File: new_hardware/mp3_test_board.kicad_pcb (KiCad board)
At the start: 4 copper layers, 100 x 56 mm, 219 parts, among them J1 TF01-A, J2 PJ-322, P1 WF24LTYAJDNN0#, P2 USB-TYPE-C-018, Q1 2N7002K, SW1 K2-1156SP-F5SW-05, SW2 K2-1156SP-F5SW-05, SW3 K2-1156SP-F5SW-05, SW4 K2-1156SP-F5SW-05, SW5 K2-1156SP-F5SW-05, SW6 GT-TC054A-H035-L1, SW7 GT-TC054A-H035-L1, SW8 GT-TC054A-H035-L1, U1 F133, U10 SGM6603-ADJYN6G, U11 SGM3204, U2 USBLC6-2SC6, U3 MX25L25645GM2I-08G, U4 PCM1795, U5 LM4562, U6 LM4562, U7 OPA1656, U8 OPA1656, U9 AXP2101, Y1 12.88727

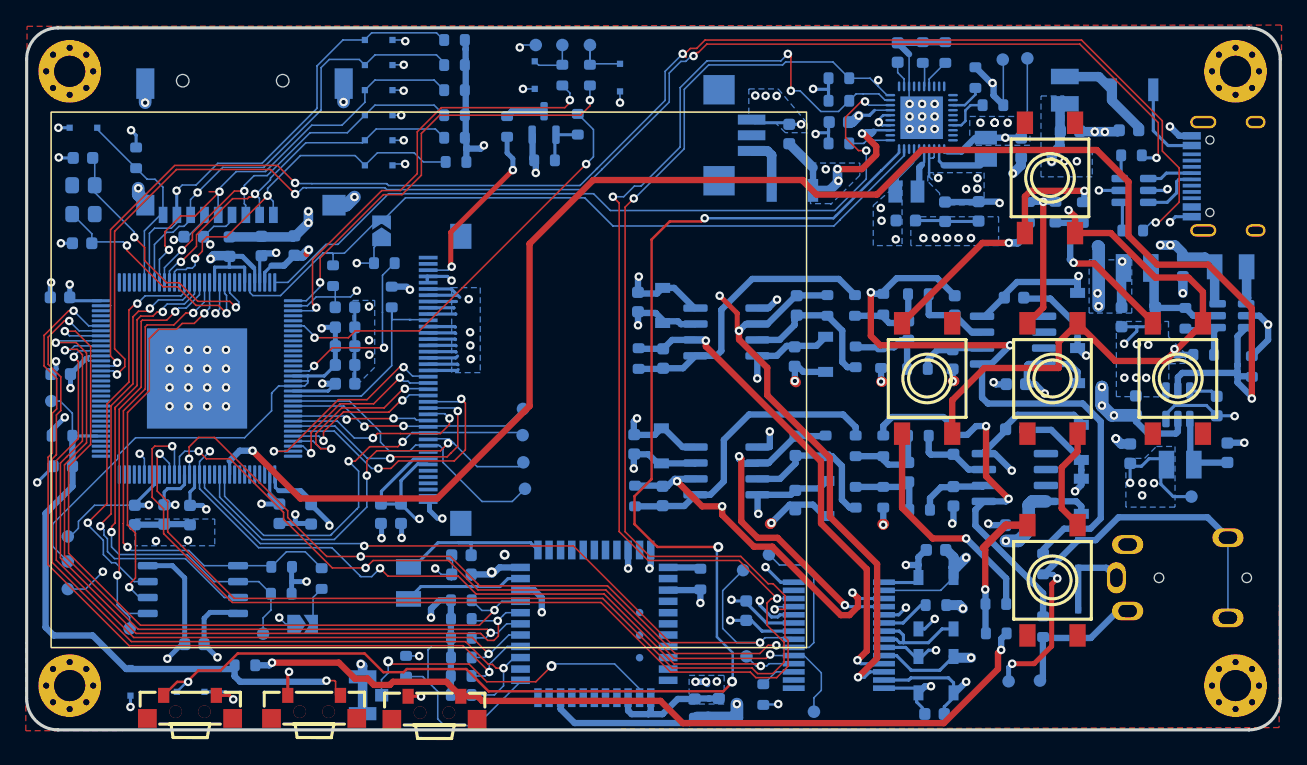
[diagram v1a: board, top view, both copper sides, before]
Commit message: wi-fi module is moved to closer board outline,unused files are removed
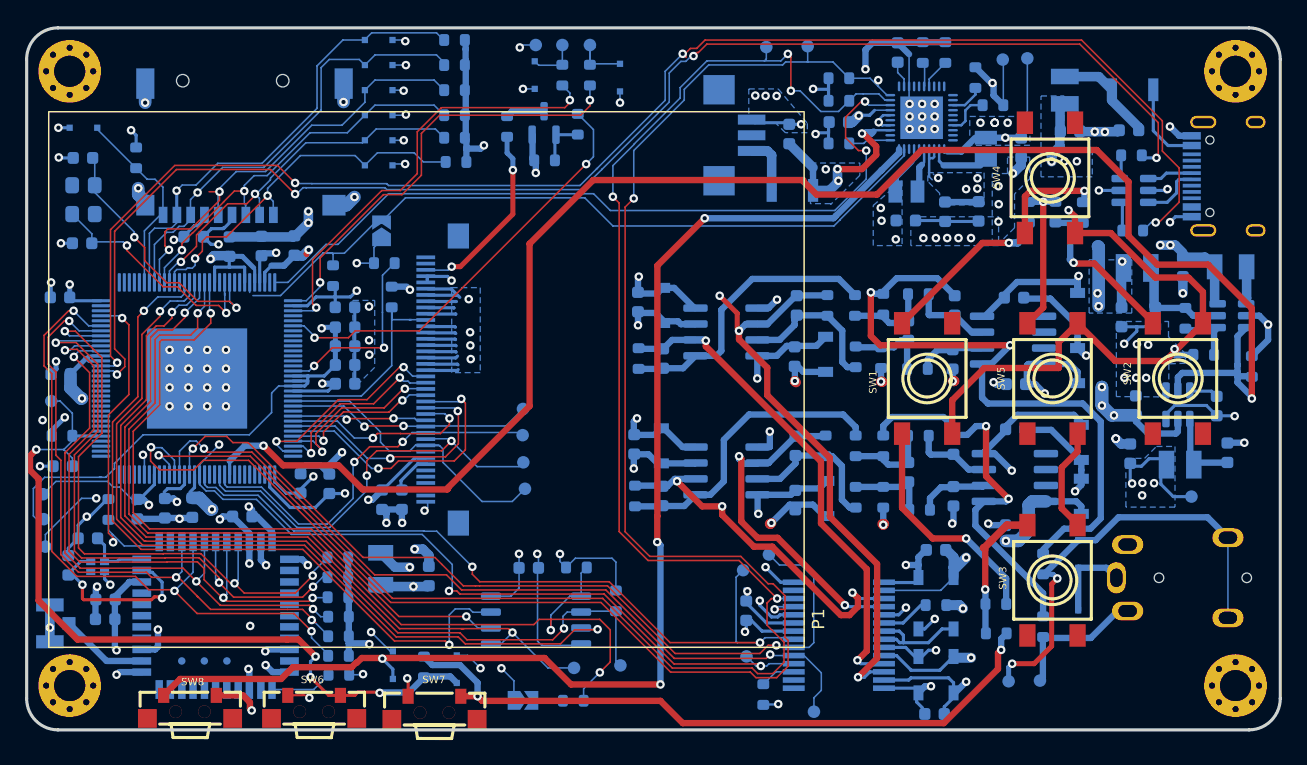
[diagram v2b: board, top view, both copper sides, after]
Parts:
- added C76: 18p, rlib_passive:C_0603_1608Metric, B.Cu at (79.8, 86.1)
- added C77: 18p, rlib_passive:C_0603_1608Metric, B.Cu at (81.4, 84.0)
- added TP24: TestPoint, TestPoint:TestPoint_Pad_D1.0mm, B.Cu at (135.5, 44.8)
- added TP25: TestPoint, TestPoint:TestPoint_Pad_D1.0mm, B.Cu at (138.8, 44.7)
- added Y2: 26МHz, rlib_passive:CRYSTAL-SMD_4P-L1.6-W1.2-BL, B.Cu at (82.1, 86.2)
- moved C56 49.7 mm to (82.8, 88.8), turned to 180 degrees
- moved C59 47.6 mm to (82.7, 90.4), turned to 180 degrees
- moved TP12 35.6 mm to (120.1, 94.3)
- moved U 30.2 mm to (91.5, 90.1), turned to 0 degrees
- moved R63 29.8 mm to (101.4, 94.8), turned to 0 degrees
- moved TP11 28.6 mm to (123.8, 94.1)
- moved U3 27.5 mm to (117.1, 90.5)
- moved C26 27.4 mm to (116.5, 86.3)
- moved R64 26.8 mm to (83.0, 81.7)
- moved R21 26.7 mm to (123.5, 88.9), turned to 90 degrees
- moved D1 26.0 mm to (110.8, 94.4), turned to -90 degrees
- moved RF1 25.6 mm to (79.1, 90.7)
- moved R17 23.5 mm to (120.3, 86.3), turned to 180 degrees
- moved R6 22.3 mm to (120.1, 96.9), turned to 0 degrees
- moved JP1 18.6 mm to (116.1, 96.9)
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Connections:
- R64 pad 1: /WI-FI/WIFI_REG_ON -> /SOC/WIFI_REG_ON
- R7 pad 1: /SOC/KEYS -> Net-(R7-Pad1)
- R7 pad 2: Net-(R7-Pad2) -> /SOC/KEYS
- R9 pad 1: Net-(R7-Pad2) -> Net-(R7-Pad1)
- SW7 pad 1: Net-(R7-Pad2) -> Net-(R7-Pad1)
- U pad 10: unconnected-(U12-Pad10) -> Net-(C76-Pad2)
- U pad 11: unconnected-(U12-Pad11) -> Net-(C77-Pad2)
- U pad 12: /WI-FI/WIFI_REG_ON -> /SOC/WIFI_REG_ON
- U1 pad 125: unconnected-(U1-Pad125) -> /SOC/WIFI_REG_ON
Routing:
- net Net-(R7-Pad2): track 66.8 -> 0.00 mm, vias 2 -> 0
- net Net-(R7-Pad1): track 0.00 -> 55.2 mm, vias 0 -> 2
- net /SOC/FLASH_SPI_CS: track 42.7 -> 79.1 mm, vias 2 -> 3
- net /SOC/FLASH_SPI_MOSI: track 34.9 -> 64.9 mm
- net /SOC/FLASH_SPI_MISO: track 43.3 -> 71.5 mm
- net /SOC/FLASH_SPI_WP: track 38.1 -> 66.3 mm
- net /SOC/FLASH_SPI_HOLD: track 31.6 -> 59.5 mm
- net /SOC/WIFI_REG_ON: track 0.00 -> 27.0 mm, vias 0 -> 2
- net /SOC/FLASH_SPI_CLK: track 30.7 -> 54.8 mm
- net /SOC/WIFI_SDIO_D2: track 69.2 -> 50.3 mm, vias 2 -> 3
- net Net-(RF1-Pad1): track 26.1 -> 7.97 mm, vias 2 -> 0
- net /WI-FI/WIFI_REG_ON: track 16.5 -> 0.00 mm
- net /SOC/WIFI_SDIO_D0: track 64.9 -> 49.1 mm, vias 2 -> 3
- net /SOC/WIFI_SDIO_CMD: track 61.7 -> 45.9 mm, vias 2 -> 3
- net /SOC/WIFI_SDIO_D1: track 64.3 -> 49.0 mm, vias 2 -> 3
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- removed copper zone on F.Cu, net GND
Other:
- board text added: "0,0889 мм / 0,0000 мм"
- board text added: "0,2000 мм"
- board text added: "1,6700 мм"
- board text added: "100,0000 мм x 56,0000 мм"
- board text added: "4"
- board text added: "None"
- board text added: "Габариты платы:"
- board text added: "Количество слоёв меди:"
- board text added: "Контроль импеданса:"
- board text added: "Краевой соединитель:"
- board text added: "Метал. торцы:"
- board text added: "Мин. дорожка/зазор:"
- board text added: "Мин. сверло:"
- board text added: "Нет"
- board text added: "Периферийные полу-отверстия:"
- board text added: "Покрытие меди:"
- board text added: "Толщина платы:"
- board text added: "ХАРАКТЕРИСТИКИ ПЛАТЫ"

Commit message: x
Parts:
- moved TP21 0.51 mm to (138.8, 98.0)
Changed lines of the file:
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@@
     (property "exclude_from_bom" "")
     (attr exclude_from_pos_files exclude_from_bom)
-    (fp_text reference "TP13" (at 0 1.448) (layer "B.SilkS")
+    (fp_text reference "TP13" (at 0.25 -1.736062) (layer "B.SilkS")
       (effects (font (size 0.6 0.6) (thickness 0.15)) (justify mirror))
     )
@@
     (property "exclude_from_bom" "")
     (attr exclude_from_pos_files exclude_from_bom)
-    (fp_text reference "TP23" (at 2.6 -0.2) (layer "B.SilkS")
+    (fp_text reference "TP23" (at 0.5304 1.612876) (layer "B.SilkS")
       (effects (font (size 0.6 0.6) (thickness 0.15)) (justify mirror))
     )
@@
     (property "exclude_from_bom" "")
     (attr exclude_from_pos_files exclude_from_bom)
-    (fp_text reference "TP22" (at 2.8 -0.4) (layer "B.SilkS")
+    (fp_text reference "TP22" (at 0.1004 1.552876) (layer "B.SilkS")
       (effects (font (size 0.6 0.6) (thickness 0.15)) (justify mirror))
     )
@@
     (property "Tolerance" "1%")
     (attr smd)
-    (fp_text reference "R23" (at 0 1.43 90) (layer "B.SilkS")
+    (fp_text reference "R23" (at 0.032876 -1.7404 90) (layer "B.SilkS")
       (effects (font (size 0.6 0.6) (thickness 0.15)) (justify mirror))
     )
@@
     (property "Voltage" "")
     (attr smd)
-    (fp_text reference "C4" (at -0.81 -4.39 90) (layer "B.SilkS")
+    (fp_text reference "C4" (at -0.006062 1.3573 90) (layer "B.SilkS")
       (effects (font (size 0.6 0.6) (thickness 0.15)) (justify mirror))
     )
@@
     (property "exclude_from_bom" "")
     (attr exclude_from_pos_files exclude_from_bom)
-    (fp_text reference "TP14" (at 0 1.448 90) (layer "B.SilkS")
+    (fp_text reference "TP14" (at 1.97 0.01) (layer "B.SilkS")
       (effects (font (size 0.6 0.6) (thickness 0.15)) (justify mirror))
     )
@@
     (property "Tolerance" "1%")
     (attr smd)
-    (fp_text reference "R9" (at 0 1.43) (layer "B.SilkS")
+    (fp_text reference "R9" (at 0.0627 1.163938) (layer "B.SilkS")
       (effects (font (size 0.6 0.6) (thickness 0.15)) (justify mirror))
     )
@@
     (property "Voltage" "")
     (attr smd)
-    (fp_text reference "C8" (at -0.82 -5.61 90) (layer "B.SilkS")
+    (fp_text reference "C8" (at 0.203938 1.3373 90) (layer "B.SilkS")
       (effects (font (size 0.6 0.6) (thickness 0.15)) (justify mirror))
     )
@@
     (property "Tolerance" "1%")
     (attr smd)
-    (fp_text reference "R53" (at 2.8 1.2) (layer "B.SilkS")
+    (fp_text reference "R53" (at 2.48 1) (layer "B.SilkS")
       (effects (font (size 0.6 0.6) (thickness 0.15)) (justify mirror))
     )
@@
     (property "Voltage" "")
     (attr smd)
-    (fp_text reference "C27" (at 2.8 0) (layer "B.SilkS")
+    (fp_text reference "C27" (at 2.8927 -0.026062) (layer "B.SilkS")
       (effects (font (size 0.6 0.6) (thickness 0.15)) (justify mirror))
     )
@@
     (property "Voltage" "")
     (attr smd)
-    (fp_text reference "C9" (at -0.82 -6.83 90) (layer "B.SilkS")
+    (fp_text reference "C9" (at 0.193938 1.4573 90) (layer "B.SilkS")
       (effects (font (size 0.6 0.6) (thickness 0.15)) (justify mirror))
     )
@@
   )
   (footprint "TestPoint:TestPoint_Pad_D1.0mm" (layer "B.Cu")
-    (at 139.2704 97.782876 180)
+    (at 138.8 97.99 180)
     (descr "SMD pad as test Point, diameter 1.0mm")
     (tags "test point SMD pad")
@@
     (property "exclude_from_bom" "")
     (attr exclude_from_pos_files exclude_from_bom)
-    (fp_text reference "TP21" (at 2.8 -0.2) (layer "B.SilkS")
+    (fp_text reference "TP21" (at 2.3204 -0.387124) (layer "B.SilkS")
       (effects (font (size 0.6 0.6) (thickness 0.15)) (justify mirror))
     )
@@
   (via (at 90.611862 76.798038) (size 0.6858) (drill 0.3302) (layers "F.Cu" "B.Cu") (net 168))
   (segment (start 88.66 78.8625) (end 88.66 77.006647) (width 0.127) (layer "B.Cu") (net 168))
-  (segment (start 139.8577 96.078938) (end 139.8577 94.678938) (width 0.127) (layer "B.Cu") (net 168))
+  (segment (start 138.8 97.136638) (end 139.8577 96.078938) (width 0.127) (layer "B.Cu") (net 168))
   (segment (start 88.66 77.006647) (end 89.474509 76.192138) (width 0.127) (layer "B.Cu") (net 168))
+  (segment (start 138.8 97.99) (end 138.8 97.136638) (width 0.127) (layer "B.Cu") (net 168))
+  (segment (start 139.8577 96.078938) (end 139.8577 94.678938) (width 0.127) (layer "B.Cu") (net 168))
   (segment (start 135.78 93.22) (end 135.863938 93.303938) (width 0.127) (layer "B.Cu") (net 168))
-  (segment (start 139.8577 94.678938) (end 138.4577 93.278938) (width 0.127) (layer "B.Cu") (net 168))
   (segment (start 90.005962 76.192138) (end 90.611862 76.798038) (width 0.127) (layer "B.Cu") (net 168))
-  (segment (start 139.2704 96.666238) (end 139.8577 96.078938) (width 0.127) (layer "B.Cu") (net 168))
-  (segment (start 139.2704 97.782876) (end 139.2704 96.666238) (width 0.127) (layer "B.Cu") (net 168))
   (segment (start 89.474509 76.192138) (end 90.005962 76.192138) (width 0.127) (layer "B.Cu") (net 168))
+  (segment (start 139.8577 94.678938) (end 138.4577 93.278938) (width 0.127) (layer "B.Cu") (net 168))
   (segment (start 135.863938 93.303938) (end 137.6577 93.303938) (width 0.127) (layer "B.Cu") (net 168))
   (segment (start 146.46 47.31) (end 146.46 47.9) (width 0.127) (layer "B.Cu") (net 173))
